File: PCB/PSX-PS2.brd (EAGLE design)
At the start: 58.5 x 61 mm, 17 parts

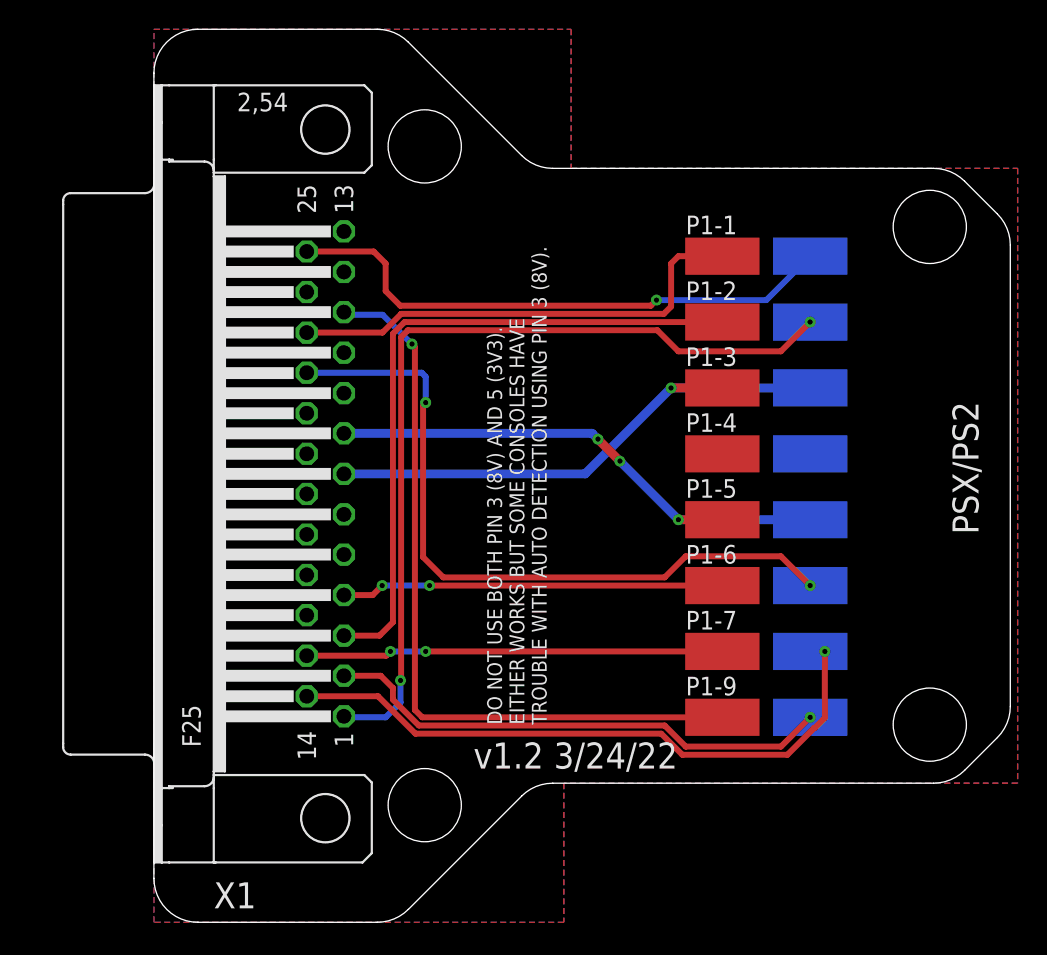
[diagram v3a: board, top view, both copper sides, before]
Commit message: PCB Update for better Housing Fit
All the PCBs were updated for better housing fitment.

Common Changes across all PCBs:
1. All Aux PCBs are now the exact same size.  (there was a .1mm-.5mm Variance previous)
2. All Aux PCBs Mounting holes are in the same location (there was a .05mm-.1mm Variance previous)
3. The DB25 has been moved 1.2mm close to the edge of the PCB for better connection when in the housing.

PCB Specific Updates:
3DO - Rename Pads (Removed trailing numbers), Flipped U2 to match U1, Moved U1 & U2 to same coordinates as other 2 Component PCBs in collection.

PCE & NES- Moved U1 & U2 to same coordinates as other 2 Component PCBs in collection.

PS2/PSX & Saturn - Added Notch on back edge of PCB for access for wires that need to attach to bottom layer of PCB.

All Gerbers have been updated.

New PCBs have been ordered for testing.
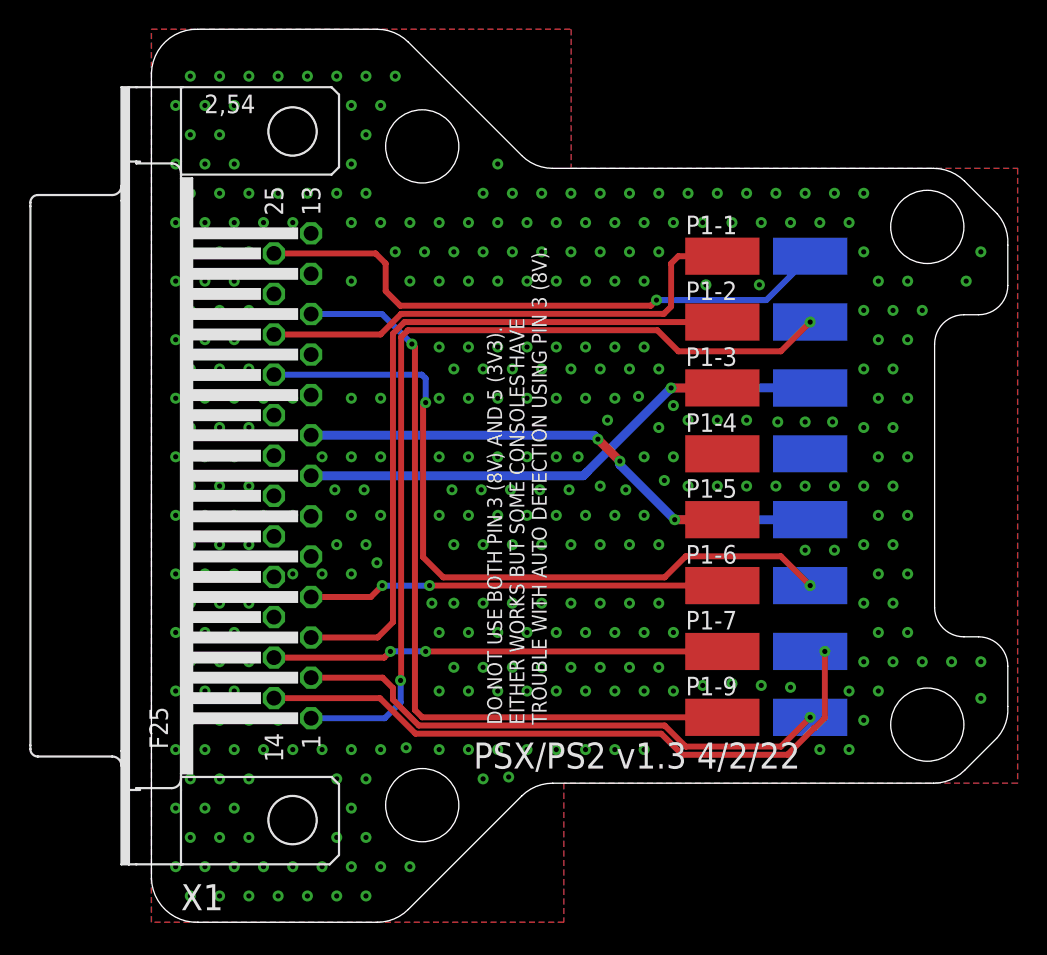
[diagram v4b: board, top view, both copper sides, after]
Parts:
- moved X1 2.24 mm to (9.64, 30.5)
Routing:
- net 3V3IN: track 37.3 -> 39.9 mm
- net IO34: track 26.1 -> 28.4 mm
- net VIN: track 37.8 -> 40.1 mm
- net IO33: track 28.5 -> 30.8 mm
- net IO19: track 32.3 -> 34.6 mm
- net IO32: track 46.3 -> 48.6 mm
- net IO27: track 58.9 -> 61.1 mm
- net IO26: track 43.6 -> 45.8 mm
- net IO21: track 51.8 -> 54.0 mm
- net IO25: track 35.1 -> 37.3 mm
- net IO22: track 38.4 -> 40.6 mm
- net IO5: track 49.1 -> 51.2 mm
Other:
- outline, holes or cut-outs redrawn
- board text added: "PSX/PS2 v1.3 4/2/22"
- board text removed: "PSX/PS2"
- board text removed: "v1.2 3/24/22"

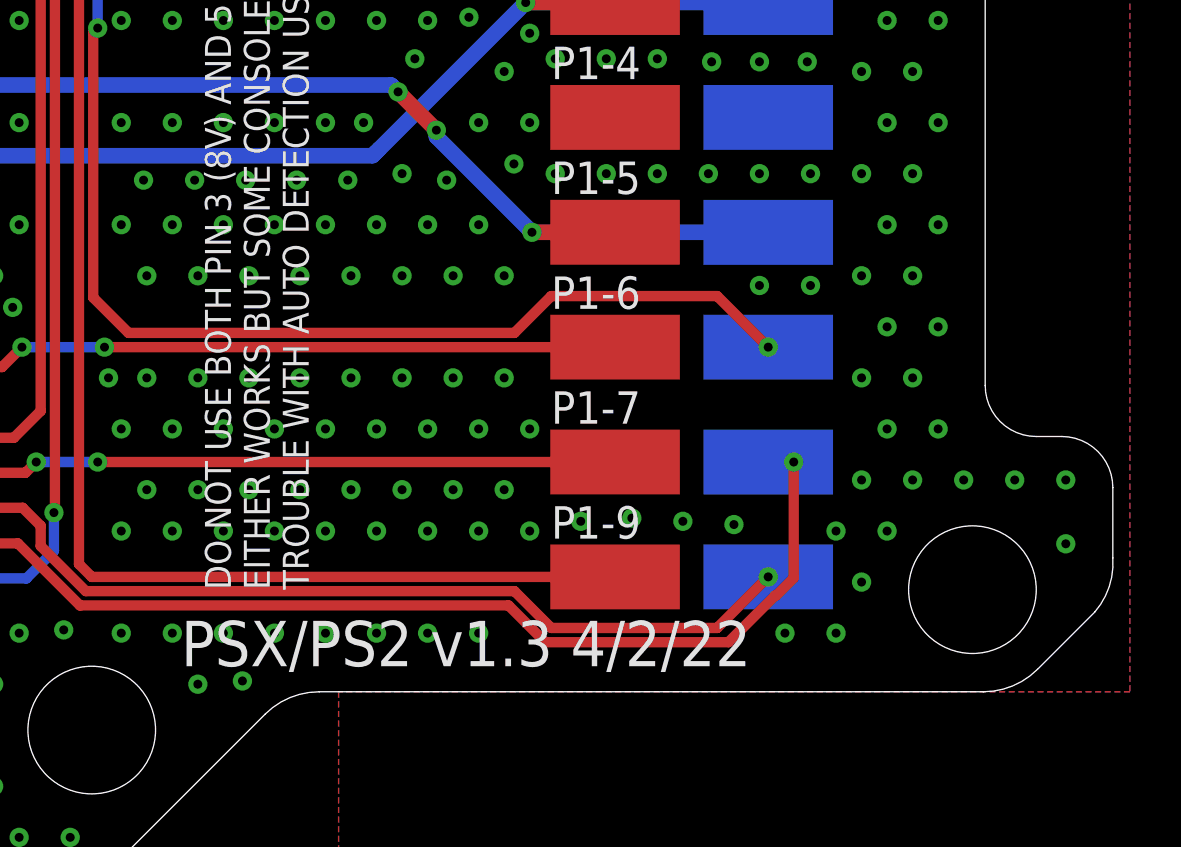
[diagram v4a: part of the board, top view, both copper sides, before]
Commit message: Updates from Issues 42/43/18
Closed Issues 42 and 43 as Sega Genesis and PSX have been successfully tested and functional.

Updated Dreamcast PCB per comment in Issue 18 - Reversed P1-P4 pads to match housing

Updated Project Status to reflect #42 and #43 Complete
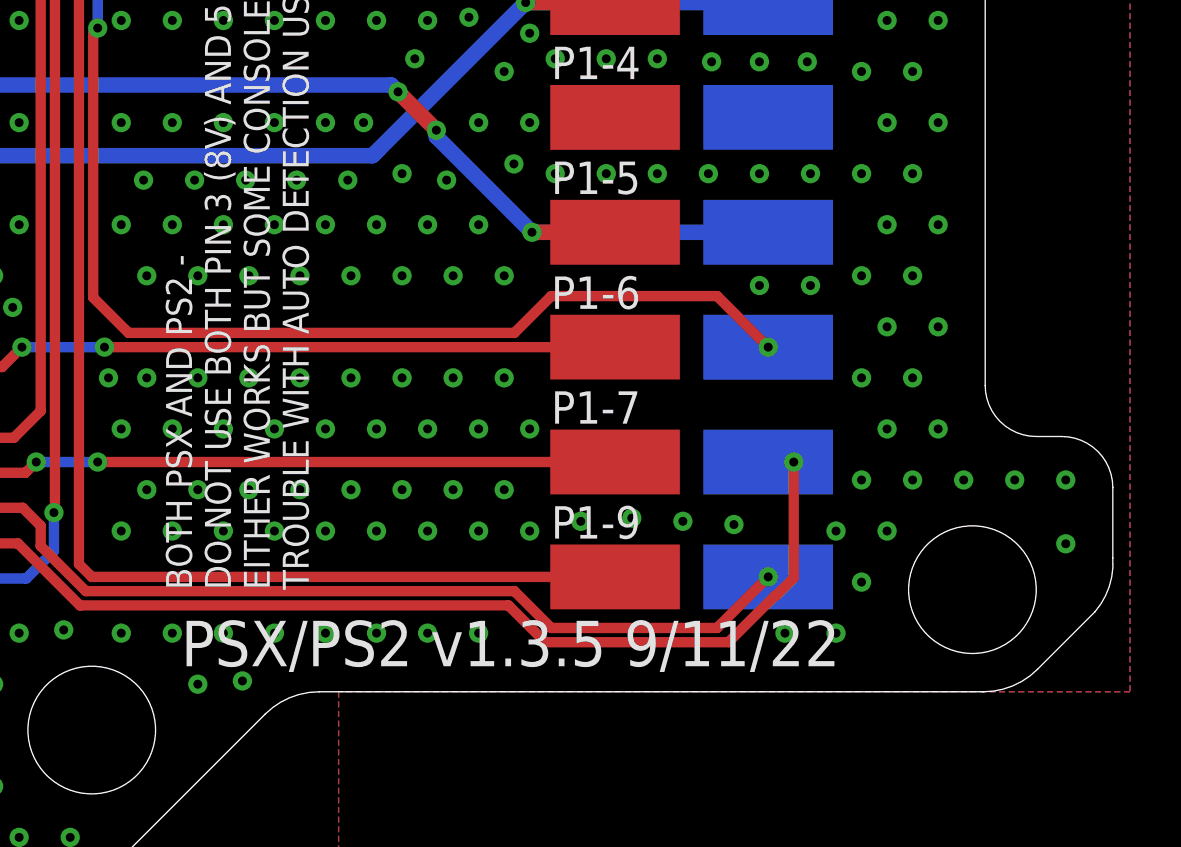
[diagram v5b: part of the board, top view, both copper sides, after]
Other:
- board text added: "BOTH PSX AND PS2 - DO NOT USE BOTH PIN 3 (8V) AND 5 (3V3). EITHER WORKS BUT SOME CONSOLES HAVE TROUBLE WITH AUTO DETECTION USING PIN 3 (8V)."
- board text added: "PSX/PS2 v1.3.5 9/11/22"
- board text removed: "DO NOT USE BOTH PIN 3 (8V) AND 5 (3V3). EITHER WORKS BUT SOME CONSOLES HAVE TROUBLE WITH AUTO DETECTION USING PIN 3 (8V)."
- board text removed: "PSX/PS2 v1.3 4/2/22"
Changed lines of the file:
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@@
 <hole x="18.5" y="53" drill="5"/>
 <hole x="18.5" y="8" drill="5"/>
-<text x="22" y="10.5" size="1.778" layer="21">PSX/PS2 v1.3 4/2/22</text>
-<text x="27" y="13.5" size="1.016" layer="25" rot="R90">DO NOT USE BOTH PIN 3 (8V) AND 5 (3V3).
+<text x="22" y="10.5" size="1.778" layer="21">PSX/PS2 v1.3.5 9/11/22</text>
+<text x="27" y="13.5" size="1.016" layer="25" rot="R90">BOTH PSX AND PS2 -
+DO NOT USE BOTH PIN 3 (8V) AND 5 (3V3).
 EITHER WORKS BUT SOME CONSOLES HAVE
 TROUBLE WITH AUTO DETECTION USING PIN 3 (8V).</text>

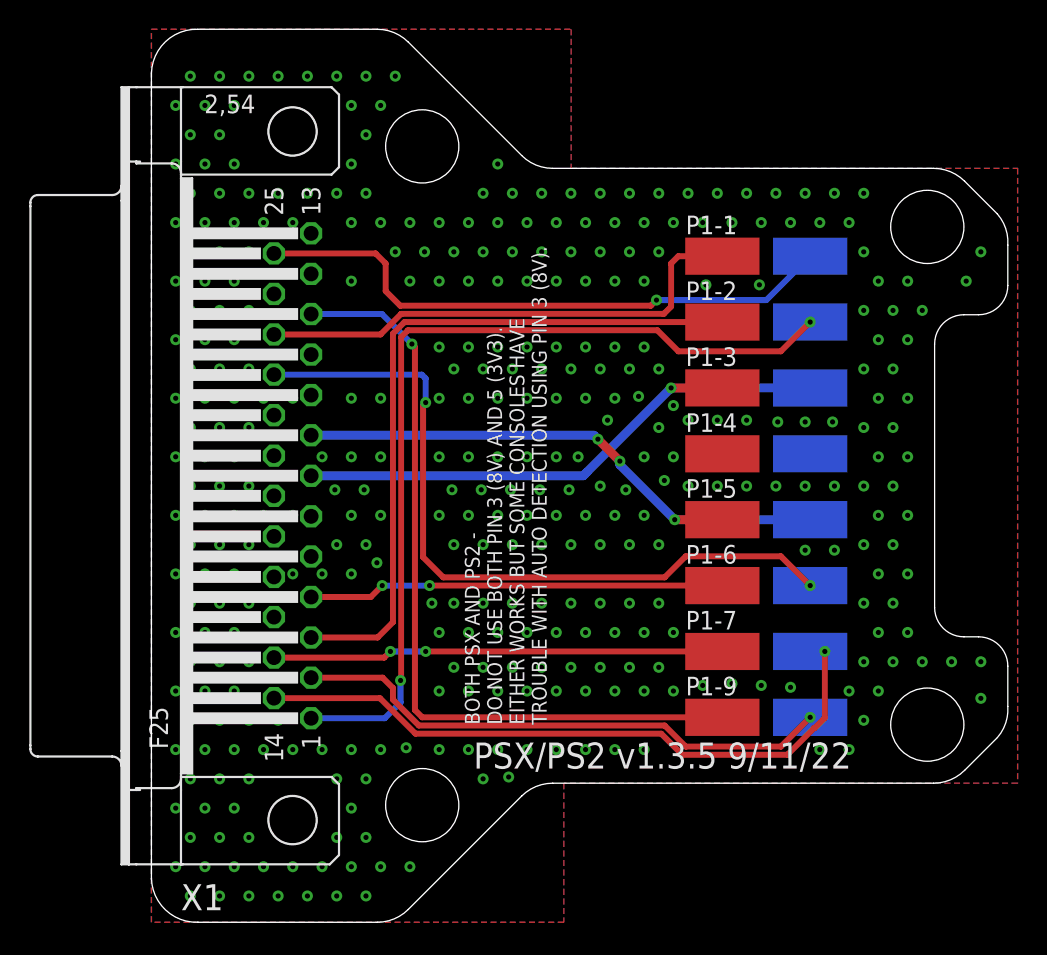
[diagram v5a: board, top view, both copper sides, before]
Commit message: Added exposed GND plane at DB25 anchors
All PCBs have been update to have exposed GND plane pads for the DB25 anchor points.

This resolves Issue 54
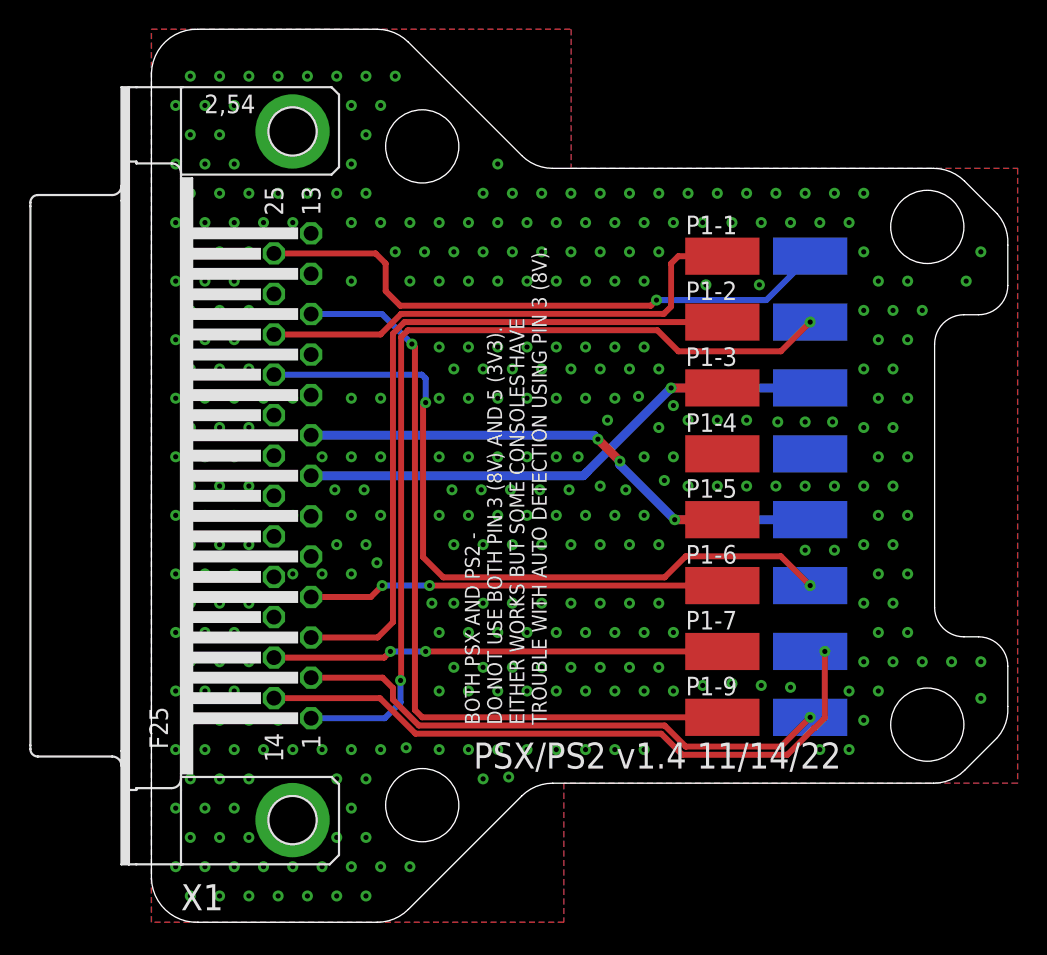
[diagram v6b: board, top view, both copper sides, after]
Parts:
- X1: device SparkFun-Retired:F25H -> SparkFun-Retired:F25HP
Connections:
- net GND: now also X1.GND1, X1.GND2
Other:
- board text added: "PSX/PS2 v1.4 11/14/22"
- board text removed: "PSX/PS2 v1.3.5 9/11/22"
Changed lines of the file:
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@@
 <hole x="18.5" y="53" drill="5"/>
 <hole x="18.5" y="8" drill="5"/>
-<text x="22" y="10.5" size="1.778" layer="21">PSX/PS2 v1.3.5 9/11/22</text>
+<text x="22" y="10.5" size="1.778" layer="21">PSX/PS2 v1.4 11/14/22</text>
 <text x="27" y="13.5" size="1.016" layer="25" rot="R90">BOTH PSX AND PS2 -
 DO NOT USE BOTH PIN 3 (8V) AND 5 (3V3).
@@
 <attribute name="VALUE" x="45" y="23" size="0.0254" layer="28" rot="MR270"/>
 </element>
-<element name="X1" library="SparkFun-Retired" package="F25H" value="" x="9.64" y="30.5" smashed="yes" rot="R90">
+<element name="X1" library="SparkFun-Retired" package="F25HP" value="" x="9.64" y="30.5" smashed="yes" rot="R90">
 <attribute name="NAME" x="4.919" y="2.6" size="1.778" layer="25" ratio="10" rot="R180"/>
 <attribute name="VALUE" x="-4.33" y="22.118" size="1.778" layer="27" ratio="10" rot="R90"/>
@@
 <via x="55.6568" y="43.7968" extent="1-16" drill="0.35"/>
 <via x="56.6568" y="45.7968" extent="1-16" drill="0.35"/>
+<contactref element="X1" pad="GND1"/>
+<contactref element="X1" pad="GND2"/>
 </signal>
 <signal name="IO5">
